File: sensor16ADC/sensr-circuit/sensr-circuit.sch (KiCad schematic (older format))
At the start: 20 parts, among them J1 Conn_01x09_Male, U1 WeMos_D1_mini, U2 CD74HC4067M, U3 AMS1117CD-1.5

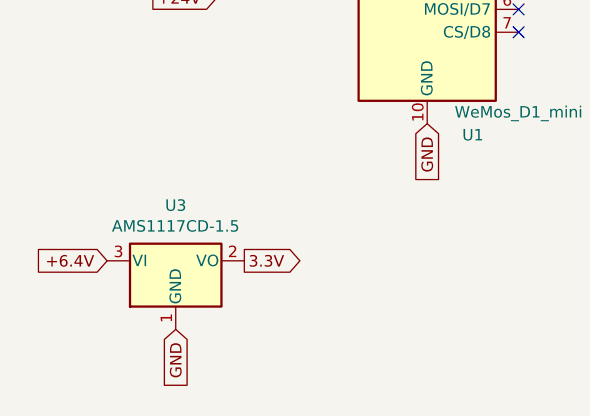
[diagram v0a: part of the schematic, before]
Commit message: circuit with 24V to 3.3V regulator
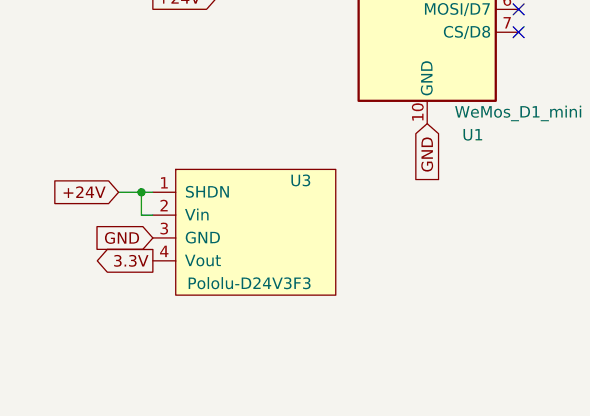
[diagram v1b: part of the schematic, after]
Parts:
- removed U3: AMS1117CD-1.5, AudioChannel:AMS1117, symbol Regulator_Linear:AMS1117CD-1.5
- added U3: Pololu-D24V3F3, AudioChannel:Pololu-D24V3F3, symbol AudioChannel-cache:Pololu-D24V3F3
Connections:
- net +24V: now also U3.1 (SHDN), U3.2 (Vin)
- net 3.3V: now also U3.4 (Vout)
- net GND: now also U3.3 (GND)
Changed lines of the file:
@@
 Text GLabel 3850 2850 0    50   Input ~ 0
 GND
-$Comp
-L Regulator_Linear:AMS1117CD-1.5 U3
-U 1 1 62369A95
-P 1500 3600
-F 0 "U3" H 1500 3842 50  0000 C CNN
-F 1 "AMS1117CD-1.5" H 1500 3751 50  0000 C CNN
-F 2 "AudioChannel:AMS1117" H 1500 3800 50  0001 C CNN
-F 3 "http://www.advanced-monolithic.com/pdf/ds1117.pdf" H 1600 3350 50  0001 C CNN
-	1    1500 3600
-	1    0    0    -1
-$EndComp
-Text GLabel 1500 3900 3    50   Input ~ 0
-GND
-Text GLabel 1200 3600 0    50   Input ~ 0
-+6.4V
-Text GLabel 1800 3600 2    50   Output ~ 0
+Text GLabel 1400 3500 0    50   Input ~ 0
+GND
+Text GLabel 1400 3600 0    50   Output ~ 0
 3.3V
 $Comp
@@
 NoConn ~ 2200 2100
 NoConn ~ 2200 2200
+Text GLabel 1250 3300 0    50   Input ~ 0
++24V
+Wire Wire Line
+	1250 3300 1350 3300
+Wire Wire Line
+	1400 3400 1350 3400
+Wire Wire Line
+	1350 3400 1350 3300
+Connection ~ 1350 3300
+Wire Wire Line
+	1350 3300 1400 3300
+$Comp
+L AudioChannel-cache:Pololu-D24V3F3 U3
+U 1 1 623A75EE
+P 1550 3150
+F 0 "U3" H 2000 3050 50  0000 L CNN
+F 1 "Pololu-D24V3F3" H 1550 2600 50  0000 L CNN
+F 2 "AudioChannel:Pololu-D24V3F3" H 1550 3150 50  0001 C CNN
+F 3 "" H 1550 3150 50  0001 C CNN
+	1    1550 3150
+	1    0    0    -1
+$EndComp
 $EndSCHEMATC

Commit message: circuit fix
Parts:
- added C1: 33uF, Capacitor_THT:CP_Radial_D5.0mm_P2.50mm, symbol Device:CP1_Small
- R1, R10, R11, R12, R13, R14, R15, R16, R2, R3, R4, R5, R6, R7, R8, R9: footprint Resistor_THT:R_Axial_DIN0204_L3.6mm_D1.6mm_P1.90mm_Vertical -> Resistor_THT:R_Axial_DIN0204_L3.6mm_D1.6mm_P7.62mm_Horizontal
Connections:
- net +12.8V: no longer R8.2
- net +16.2V: no longer R10.2
- net +19.4V: no longer R12.2
- net +22.6: no longer R14.2
- net +24V: now also C1.1; no longer R16.2
- net +3.2V: no longer R2.2
- net +6.4V: no longer R4.2
- net +9.6V: no longer R6.2
- net GND: now also C1.2
- net at R15.2, U2.2 (I7): now also R16.2
- net at R13.2, U2.3 (I6): now also R14.2
- net at R11.2, U2.4 (I5): now also R12.2
- net at R9.2, U2.5 (I4): now also R10.2
- net at R7.2, U2.6 (I3): now also R8.2
- net at R5.2, U2.7 (I2): now also R6.2
- net at R3.2, U2.8 (I1): now also R4.2
- net at R1.2, U2.9 (I0): now also R2.2
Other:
- moved on the sheet: R1, R10, R11, R12, R13, R14, R15, R16, R2, R3, R4, R5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

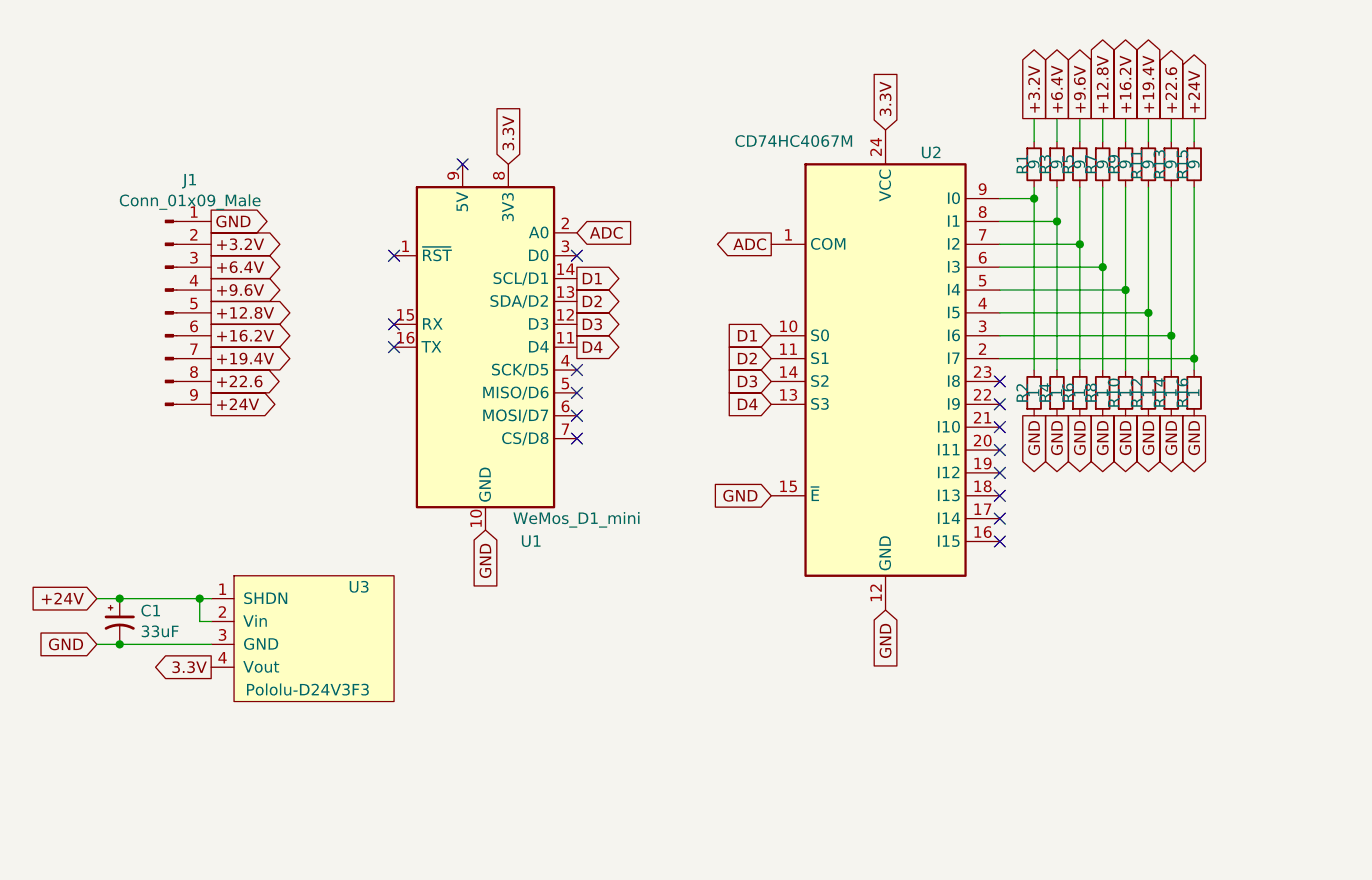
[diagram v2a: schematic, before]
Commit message: bat-mon-firmware:0.5.0 Temperature sensor DS18B20
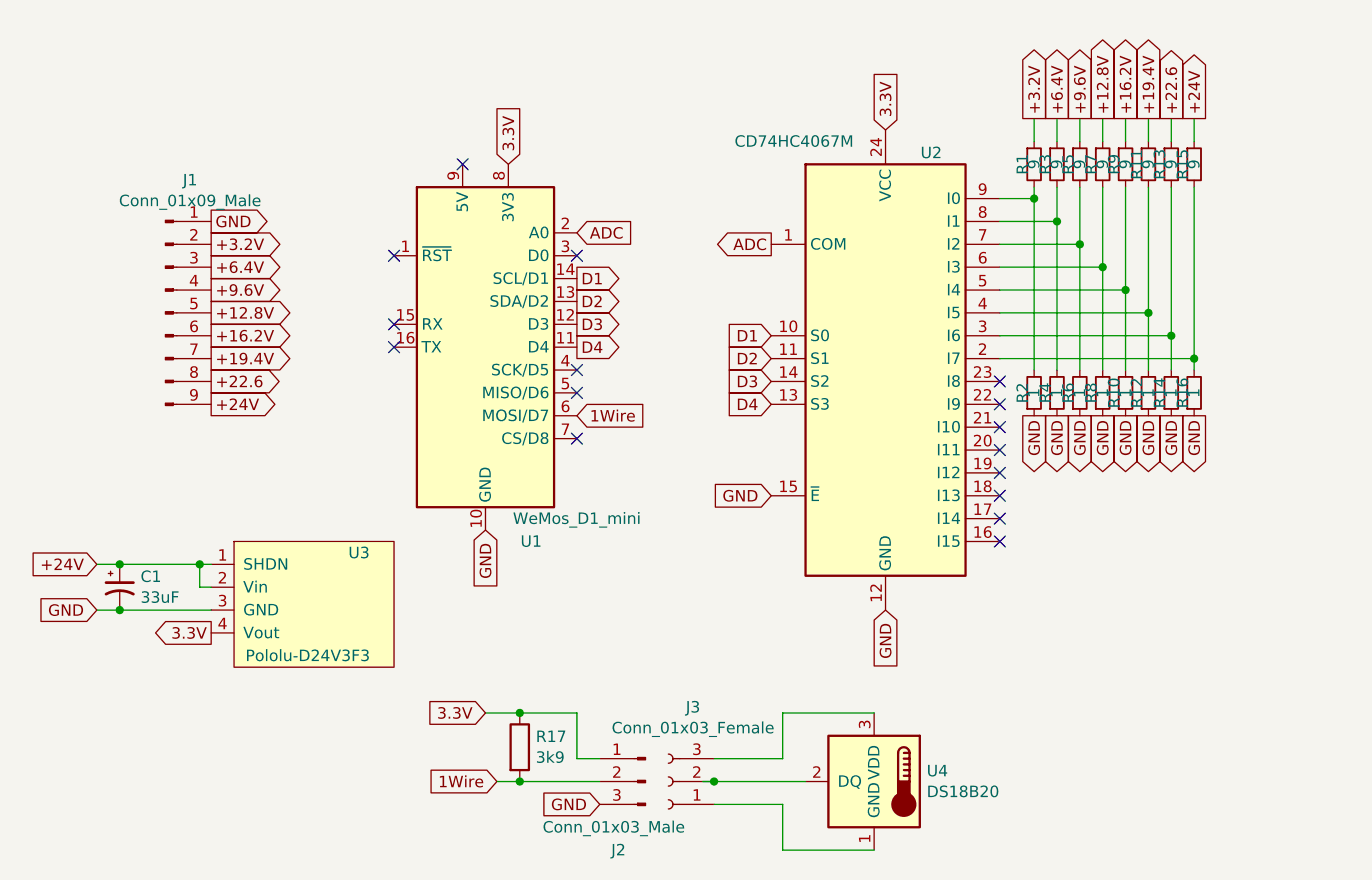
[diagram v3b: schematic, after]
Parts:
- added J2: Conn_01x03_Male, Connector_JST:JST_EH_B3B-EH-A_1x03_P2.50mm_Vertical, symbol Connector:Conn_01x03_Male
- added J3: Conn_01x03_Female, symbol Connector:Conn_01x03_Female
- added R17: 3k9, Resistor_THT:R_Axial_DIN0309_L9.0mm_D3.2mm_P2.54mm_Vertical, symbol Device:R
- added U4: DS18B20, symbol Sensor_Temperature:DS18B20
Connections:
- net 3.3V: now also J2.1 (Pin_1), R17.1
- net GND: now also J2.3 (Pin_3)
- net 1Wire: now reaches U1.6 (MOSI/D7)
- net 1Wire: now also J2.2 (Pin_2), R17.2
- new net: J3.1 (Pin_1), U4.1 (GND)
- new net: J3.2 (Pin_2), U4.2 (DQ)
- new net: J3.3 (Pin_3), U4.3 (VDD)
- no-connect marks 17 -> 16
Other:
- moved on the sheet: C1, U3
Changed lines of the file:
@@
 encoding utf-8
 Sheet 1 1
-Title ""
-Date ""
-Rev ""
-Comp ""
+Title "PV Battery Monitoring Sensor"
+Date "2022-04-04"
+Rev "1.0"
+Comp "ma-ha"
 Comment1 ""
 Comment2 ""
@@
 Text GLabel 3850 2850 0    50   Input ~ 0
 GND
-Text GLabel 900  3500 0    50   Input ~ 0
-GND
-Text GLabel 1400 3600 0    50   Output ~ 0
+Text GLabel 900  3350 0    50   Input ~ 0
+GND
+Text GLabel 1400 3450 0    50   Output ~ 0
 3.3V
 $Comp
@@
 NoConn ~ 3000 2300
 NoConn ~ 3000 2400
-NoConn ~ 3000 2500
 NoConn ~ 3000 2600
 NoConn ~ 2500 1400
@@
 NoConn ~ 2200 2100
 NoConn ~ 2200 2200
-Text GLabel 900  3300 0    50   Input ~ 0
+Text GLabel 900  3150 0    50   Input ~ 0
 +24V
 Wire Wire Line
-	900  3300 1000 3300
-Wire Wire Line
-	1400 3400 1350 3400
-Wire Wire Line
-	1350 3400 1350 3300
-Connection ~ 1350 3300
-Wire Wire Line
-	1350 3300 1400 3300
+	900  3150 1000 3150
+Wire Wire Line
+	1400 3250 1350 3250
+Wire Wire Line
+	1350 3250 1350 3150
+Connection ~ 1350 3150
+Wire Wire Line
+	1350 3150 1400 3150
 $Comp
 L AudioChannel-cache:Pololu-D24V3F3 U3
 U 1 1 623A75EE
-P 1550 3150
-F 0 "U3" H 2000 3050 50  0000 L CNN
-F 1 "Pololu-D24V3F3" H 1550 2600 50  0000 L CNN
-F 2 "AudioChannel:Pololu-D24V3F3" H 1550 3150 50  0001 C CNN
-F 3 "" H 1550 3150 50  0001 C CNN
-	1    1550 3150
+P 1550 3000
+F 0 "U3" H 2000 2900 50  0000 L CNN
+F 1 "Pololu-D24V3F3" H 1550 2450 50  0000 L CNN
+F 2 "AudioChannel:Pololu-D24V3F3" H 1550 3000 50  0001 C CNN
+F 3 "" H 1550 3000 50  0001 C CNN
+	1    1550 3000
 	1    0    0    -1
 $EndComp
@@
 Connection ~ 5600 2150
 Wire Wire Line
-	1400 3500 1000 3500
+	1400 3350 1000 3350
 $Comp
 L Device:CP1_Small C1
 U 1 1 62425038
-P 1000 3400
-F 0 "C1" H 1091 3446 50  0000 L CNN
-F 1 "33uF" H 1091 3355 50  0000 L CNN
-F 2 "Capacitor_THT:CP_Radial_D5.0mm_P2.50mm" H 1000 3400 50  0001 C CNN
-F 3 "~" H 1000 3400 50  0001 C CNN
-	1    1000 3400
-	1    0    0    -1
-$EndComp
-Connection ~ 1000 3300
-Wire Wire Line
-	1000 3300 1350 3300
-Connection ~ 1000 3500
-Wire Wire Line
-	1000 3500 900  3500
+P 1000 3250
+F 0 "C1" H 1091 3296 50  0000 L CNN
+F 1 "33uF" H 1091 3205 50  0000 L CNN
+F 2 "Capacitor_THT:CP_Radial_D5.0mm_P2.50mm" H 1000 3250 50  0001 C CNN
+F 3 "~" H 1000 3250 50  0001 C CNN
+	1    1000 3250
+	1    0    0    -1
+$EndComp
+Connection ~ 1000 3150
+Wire Wire Line
+	1000 3150 1350 3150
+Connection ~ 1000 3350
+Wire Wire Line
+	1000 3350 900  3350
 Wire Wire Line
 	5700 2300 5700 2250
 Connection ~ 5700 2250
+$Comp
+L Sensor_Temperature:DS18B20 U4
+U 1 1 624B7EB1
+P 4300 4100
+F 0 "U4" H 4070 4146 50  0000 R CNN
+F 1 "DS18B20" H 4070 4055 50  0000 R CNN
+F 2 "" H 3300 3850 50  0001 C CNN
+F 3 "http://datasheets.maximintegrated.com/en/ds/DS18B20.pdf" H 4150 4350 50  0001 C CNN
+	1    4300 4100
+	-1   0    0    -1
+$EndComp
+$Comp
+L Connector:Conn_01x03_Male J2
+U 1 1 624B8442
+P 3300 4100
+F 0 "J2" H 3450 3800 50  0000 R CNN
+F 1 "Conn_01x03_Male" H 3750 3900 50  0000 R CNN
+F 2 "Connector_JST:JST_EH_B3B-EH-A_1x03_P2.50mm_Vertical" H 3300 4100 50  0001 C CNN
+F 3 "~" H 3300 4100 50  0001 C CNN
+	1    3300 4100
+	-1   0    0    -1
+$EndComp
+$Comp
+L Connector:Conn_01x03_Female J3
+U 1 1 624B8AFD
+P 3400 4100
+F 0 "J3" H 3292 3775 50  0000 C CNN
+F 1 "Conn_01x03_Female" H 3292 3866 50  0000 C CNN
+F 2 "" H 3400 4100 50  0001 C CNN
+F 3 "~" H 3400 4100 50  0001 C CNN
+	1    3400 4100
+	-1   0    0    1
+$EndComp
+Wire Wire Line
+	3600 4200 3900 4200
+Wire Wire Line
+	3900 4200 3900 4400
+Wire Wire Line
+	3900 4400 4300 4400
+Wire Wire Line
+	4300 3800 3900 3800
+Wire Wire Line
+	3900 3800 3900 4000
+Wire Wire Line
+	3900 4000 3600 4000
+Wire Wire Line
+	3550 4100 3600 4100
+Connection ~ 3600 4100
+Wire Wire Line
+	3600 4100 4000 4100
+Text GLabel 3100 4200 0    50   Input ~ 0
+GND
+Text GLabel 2600 3800 0    50   Input ~ 0
+3.3V
+Text GLabel 3000 2500 2    50   Input ~ 0
+1Wire
+Text GLabel 2650 4100 0    50   Input ~ 0
+1Wire
+$Comp
+L Device:R R17
+U 1 1 624CAB9E
+P 2750 3950
+F 0 "R17" H 2820 3996 50  0000 L CNN
+F 1 "3k9" H 2820 3905 50  0000 L CNN
+F 2 "Resistor_THT:R_Axial_DIN0309_L9.0mm_D3.2mm_P2.54mm_Vertical" V 2680 3950 50  0001 C CNN
+F 3 "~" H 2750 3950 50  0001 C CNN
+	1    2750 3950
+	1    0    0    -1
+$EndComp
+Wire Wire Line
+	2600 3800 2750 3800
+Wire Wire Line
+	3000 3800 3000 4000
+Wire Wire Line
+	3000 4000 3100 4000
+Connection ~ 2750 3800
+Wire Wire Line
+	2750 3800 3000 3800
+Wire Wire Line
+	3100 4100 2750 4100
+Connection ~ 2750 4100
+Wire Wire Line
+	2750 4100 2650 4100
 $EndSCHEMATC
